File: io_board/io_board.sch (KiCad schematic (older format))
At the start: 0 parts

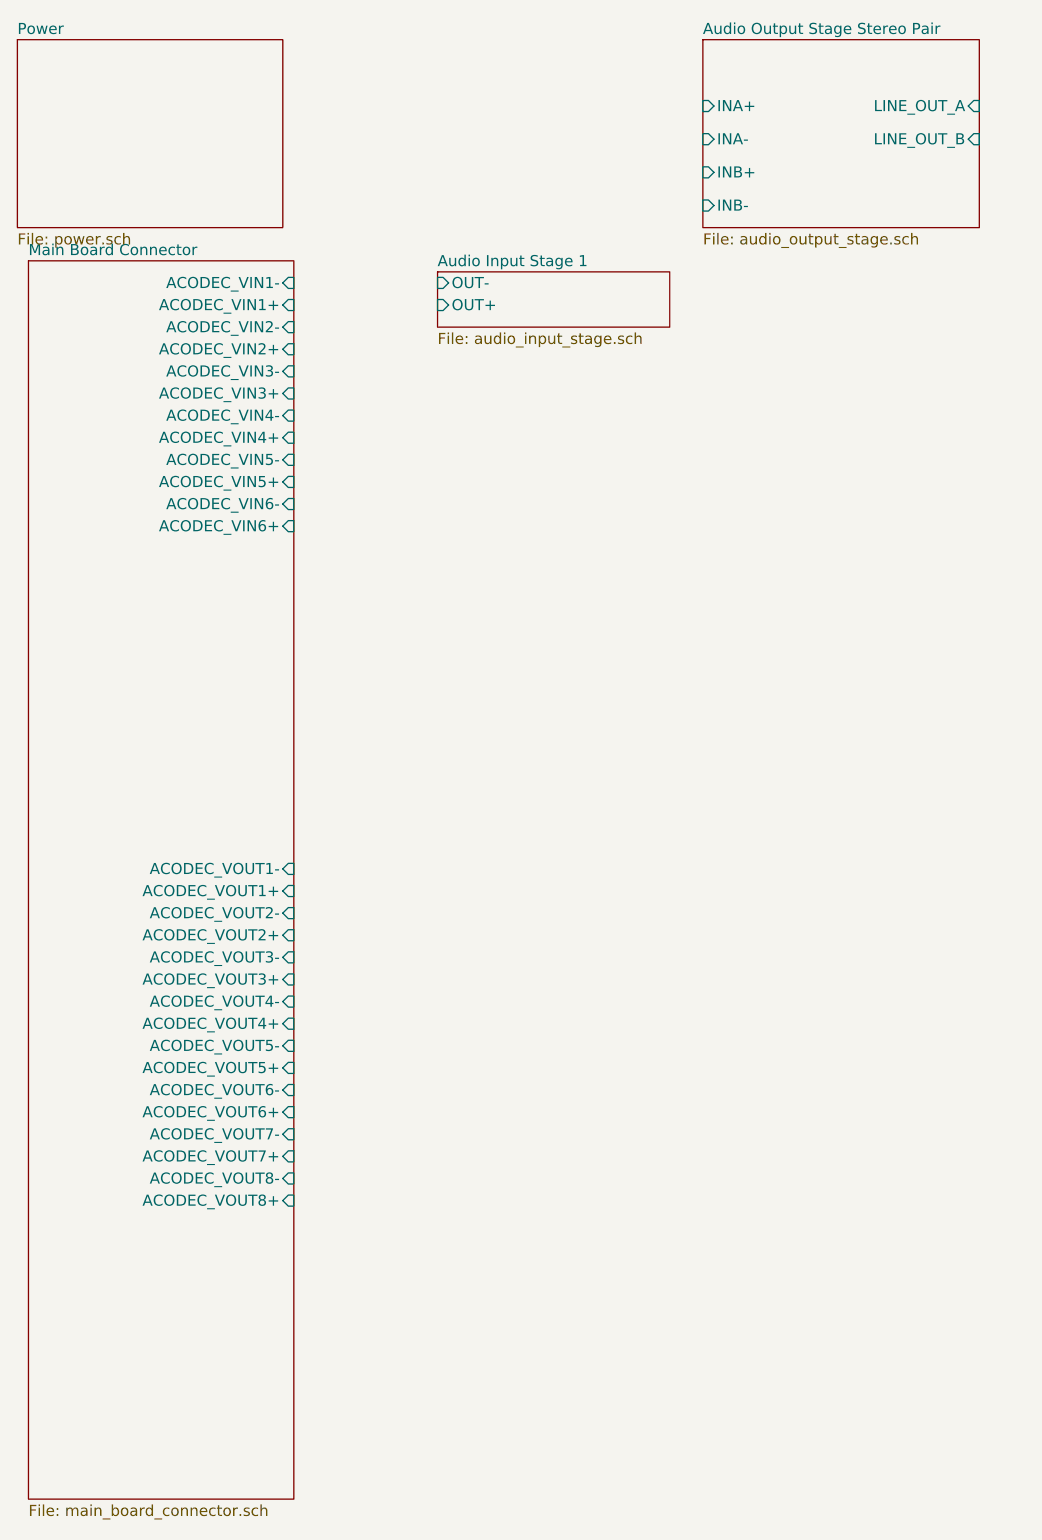
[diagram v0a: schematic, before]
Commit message: Added MIDI connectors and SD card to io_board
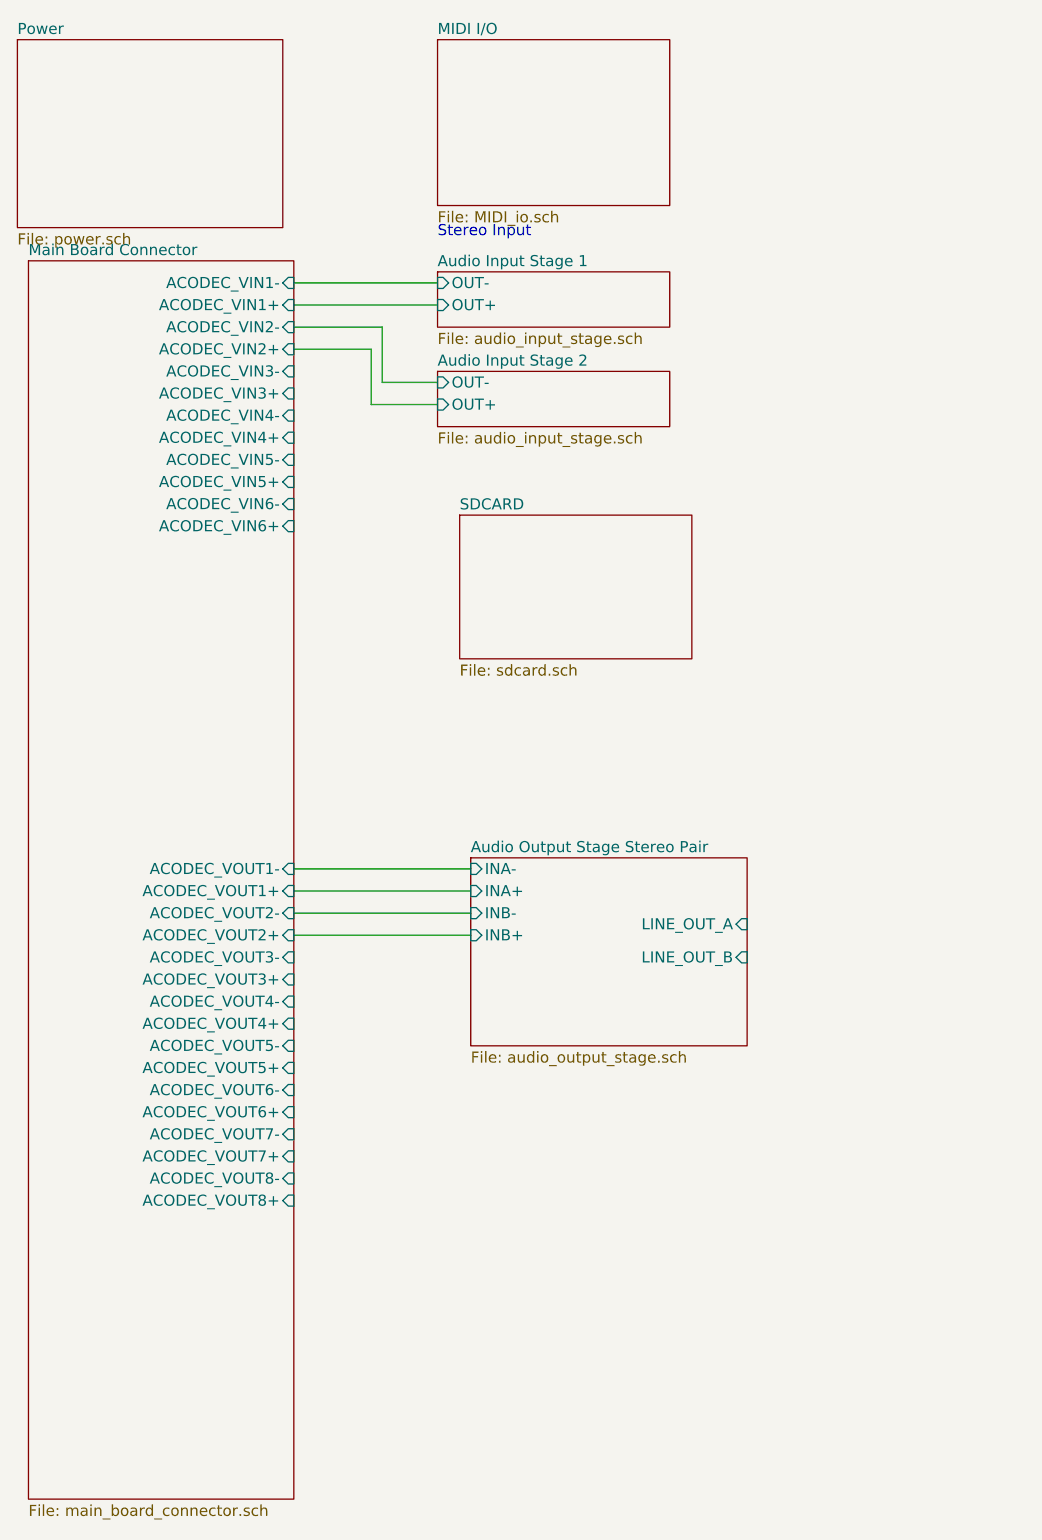
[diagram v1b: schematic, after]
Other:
- note added: "Stereo Input"
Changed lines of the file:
@@
 EESchema Schematic File Version 4
 LIBS:io_board-cache
-EELAYER 26 0
+EELAYER 29 0
 EELAYER END
 $Descr A4 11693 8268
 encoding utf-8
-Sheet 1 5
+Sheet 1 8
 Title ""
 Date ""
@@
 $EndSheet
 $Sheet
-S 4200 1000 1250 850
+S 3150 4700 1250 850
 U 5D3F56F3
 F0 "Audio Output Stage Stereo Pair" 50
 F1 "audio_output_stage.sch" 50
-F2 "INA+" I L 4200 1300 50
-F3 "INA-" I L 4200 1450 50
-F4 "LINE_OUT_A" I R 5450 1300 50
-F5 "INB+" I L 4200 1600 50
-F6 "INB-" I L 4200 1750 50
-F7 "LINE_OUT_B" I R 5450 1450 50
+F2 "INA+" I L 3150 4850 50
+F3 "INA-" I L 3150 4750 50
+F4 "LINE_OUT_A" I R 4400 5000 50
+F5 "INB+" I L 3150 5050 50
+F6 "INB-" I L 3150 4950 50
+F7 "LINE_OUT_B" I R 4400 5150 50
 $EndSheet
 $Sheet
@@
 F29 "ACODEC_VOUT1-" I R 2350 4750 50
 $EndSheet
+$Sheet
+S 3000 2500 1050 250
+U 5D3F163F
+F0 "Audio Input Stage 2" 50
+F1 "audio_input_stage.sch" 50
+F2 "OUT+" I L 3000 2650 50
+F3 "OUT-" I L 3000 2550 50
+$EndSheet
+Text Notes 3000 1900 0    50   ~ 0
+Stereo Input
+Wire Wire Line
+	2350 2100 3000 2100
+Wire Wire Line
+	2350 2200 3000 2200
+Wire Wire Line
+	2350 2300 2750 2300
+Wire Wire Line
+	2750 2300 2750 2550
+Wire Wire Line
+	2750 2550 3000 2550
+Wire Wire Line
+	2350 2400 2700 2400
+Wire Wire Line
+	2700 2400 2700 2650
+Wire Wire Line
+	2700 2650 3000 2650
+Wire Wire Line
+	2350 4750 3150 4750
+Wire Wire Line
+	2350 4850 3150 4850
+Wire Wire Line
+	2350 4950 3150 4950
+Wire Wire Line
+	2350 5050 3150 5050
+$Sheet
+S 3000 1000 1050 750
+U 5D434222
+F0 "MIDI I/O" 50
+F1 "MIDI_io.sch" 50
+$EndSheet
+$Sheet
+S 3100 3150 1050 650
+U 5D472DBF
+F0 "SDCARD" 50
+F1 "sdcard.sch" 50
+$EndSheet
 $EndSCHEMATC

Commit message: Added encoders, started adding CV input stage.
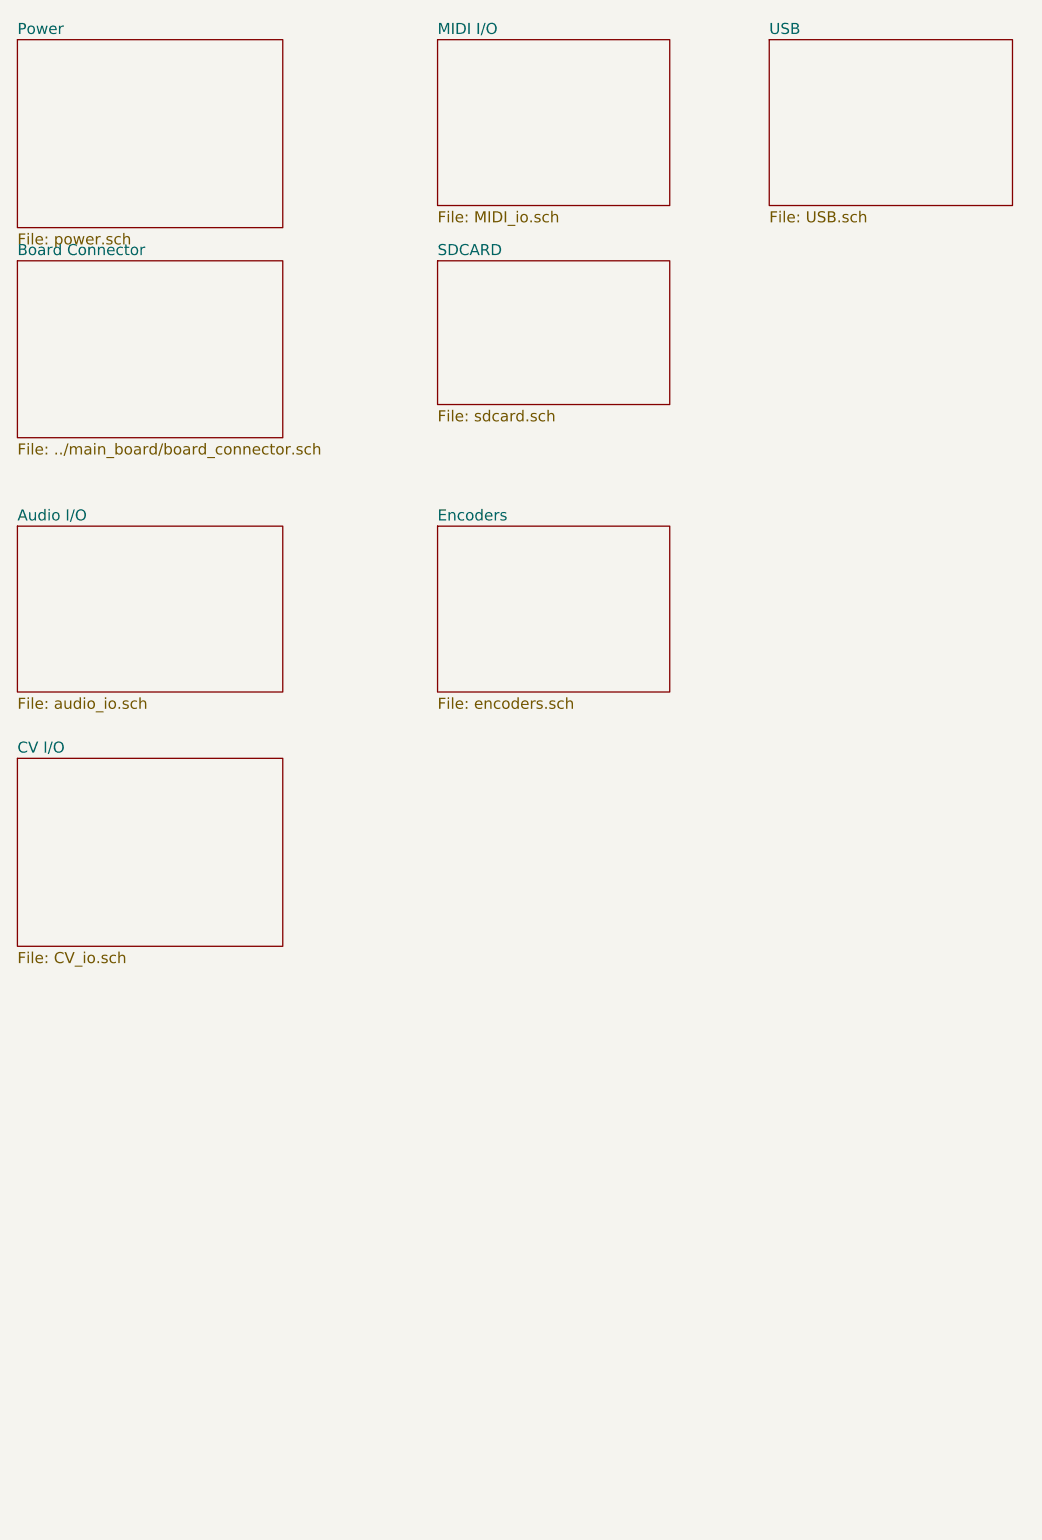
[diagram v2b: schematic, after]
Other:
- note removed: "Stereo Input"
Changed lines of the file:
@@
 $Descr A4 11693 8268
 encoding utf-8
-Sheet 1 8
+Sheet 1 12
 Title ""
 Date ""
@@
 $EndSheet
 $Sheet
-S 3000 2050 1050 250
-U 5D3A0EFE
-F0 "Audio Input Stage 1" 50
-F1 "audio_input_stage.sch" 50
-F2 "OUT+" I L 3000 2200 50
-F3 "OUT-" I L 3000 2100 50
-$EndSheet
-$Sheet
-S 3150 4700 1250 850
-U 5D3F56F3
-F0 "Audio Output Stage Stereo Pair" 50
-F1 "audio_output_stage.sch" 50
-F2 "INA+" I L 3150 4850 50
-F3 "INA-" I L 3150 4750 50
-F4 "LINE_OUT_A" I R 4400 5000 50
-F5 "INB+" I L 3150 5050 50
-F6 "INB-" I L 3150 4950 50
-F7 "LINE_OUT_B" I R 4400 5150 50
-$EndSheet
-$Sheet
-S 1150 2000 1200 5600
-U 5D43BE69
-F0 "Main Board Connector" 50
-F1 "main_board_connector.sch" 50
-F2 "ACODEC_VOUT1+" I R 2350 4850 50
-F3 "ACODEC_VOUT2-" I R 2350 4950 50
-F4 "ACODEC_VOUT2+" I R 2350 5050 50
-F5 "ACODEC_VOUT3-" I R 2350 5150 50
-F6 "ACODEC_VOUT3+" I R 2350 5250 50
-F7 "ACODEC_VOUT4-" I R 2350 5350 50
-F8 "ACODEC_VOUT4+" I R 2350 5450 50
-F9 "ACODEC_VOUT5-" I R 2350 5550 50
-F10 "ACODEC_VOUT5+" I R 2350 5650 50
-F11 "ACODEC_VOUT6-" I R 2350 5750 50
-F12 "ACODEC_VOUT6+" I R 2350 5850 50
-F13 "ACODEC_VOUT7-" I R 2350 5950 50
-F14 "ACODEC_VOUT7+" I R 2350 6050 50
-F15 "ACODEC_VOUT8-" I R 2350 6150 50
-F16 "ACODEC_VOUT8+" I R 2350 6250 50
-F17 "ACODEC_VIN3-" I R 2350 2500 50
-F18 "ACODEC_VIN3+" I R 2350 2600 50
-F19 "ACODEC_VIN4-" I R 2350 2700 50
-F20 "ACODEC_VIN4+" I R 2350 2800 50
-F21 "ACODEC_VIN5-" I R 2350 2900 50
-F22 "ACODEC_VIN5+" I R 2350 3000 50
-F23 "ACODEC_VIN6-" I R 2350 3100 50
-F24 "ACODEC_VIN6+" I R 2350 3200 50
-F25 "ACODEC_VIN1-" I R 2350 2100 50
-F26 "ACODEC_VIN1+" I R 2350 2200 50
-F27 "ACODEC_VIN2-" I R 2350 2300 50
-F28 "ACODEC_VIN2+" I R 2350 2400 50
-F29 "ACODEC_VOUT1-" I R 2350 4750 50
-$EndSheet
-$Sheet
-S 3000 2500 1050 250
-U 5D3F163F
-F0 "Audio Input Stage 2" 50
-F1 "audio_input_stage.sch" 50
-F2 "OUT+" I L 3000 2650 50
-F3 "OUT-" I L 3000 2550 50
-$EndSheet
-Text Notes 3000 1900 0    50   ~ 0
-Stereo Input
-Wire Wire Line
-	2350 2100 3000 2100
-Wire Wire Line
-	2350 2200 3000 2200
-Wire Wire Line
-	2350 2300 2750 2300
-Wire Wire Line
-	2750 2300 2750 2550
-Wire Wire Line
-	2750 2550 3000 2550
-Wire Wire Line
-	2350 2400 2700 2400
-Wire Wire Line
-	2700 2400 2700 2650
-Wire Wire Line
-	2700 2650 3000 2650
-Wire Wire Line
-	2350 4750 3150 4750
-Wire Wire Line
-	2350 4850 3150 4850
-Wire Wire Line
-	2350 4950 3150 4950
-Wire Wire Line
-	2350 5050 3150 5050
-$Sheet
 S 3000 1000 1050 750
 U 5D434222
@@
 $EndSheet
 $Sheet
-S 3100 3150 1050 650
+S 3000 2000 1050 650
 U 5D472DBF
 F0 "SDCARD" 50
 F1 "sdcard.sch" 50
 $EndSheet
+$Sheet
+S 4500 1000 1100 750
+U 5D436844
+F0 "USB" 50
+F1 "USB.sch" 50
+$EndSheet
+$Sheet
+S 1100 3200 1200 750
+U 5D487103
+F0 "Audio I/O" 50
+F1 "audio_io.sch" 50
+$EndSheet
+$Sheet
+S 1100 2000 1200 800
+U 5D446F08
+F0 "Board Connector" 50
+F1 "../main_board/board_connector.sch" 50
+$EndSheet
+$Sheet
+S 3000 3200 1050 750
+U 5D44A871
+F0 "Encoders" 50
+F1 "encoders.sch" 50
+$EndSheet
+$Sheet
+S 1100 4250 1200 850
+U 5D47B036
+F0 "CV I/O" 50
+F1 "CV_io.sch" 50
+$EndSheet
 $EndSCHEMATC
